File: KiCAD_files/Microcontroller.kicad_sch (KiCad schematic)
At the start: 71 parts, among them J403 RJ45_LED_Shielded, J404 RJ45_LED_Shielded, J405 Conn_01x02_Male, J406 Conn_01x02_Male, P401 Power2, U401 OwnTech_SPIN, U402 TCAN334GDR, U405 LTC2850xS8, U406 MCP6487T-E/SN, U407 MCP6486UT-E/LT

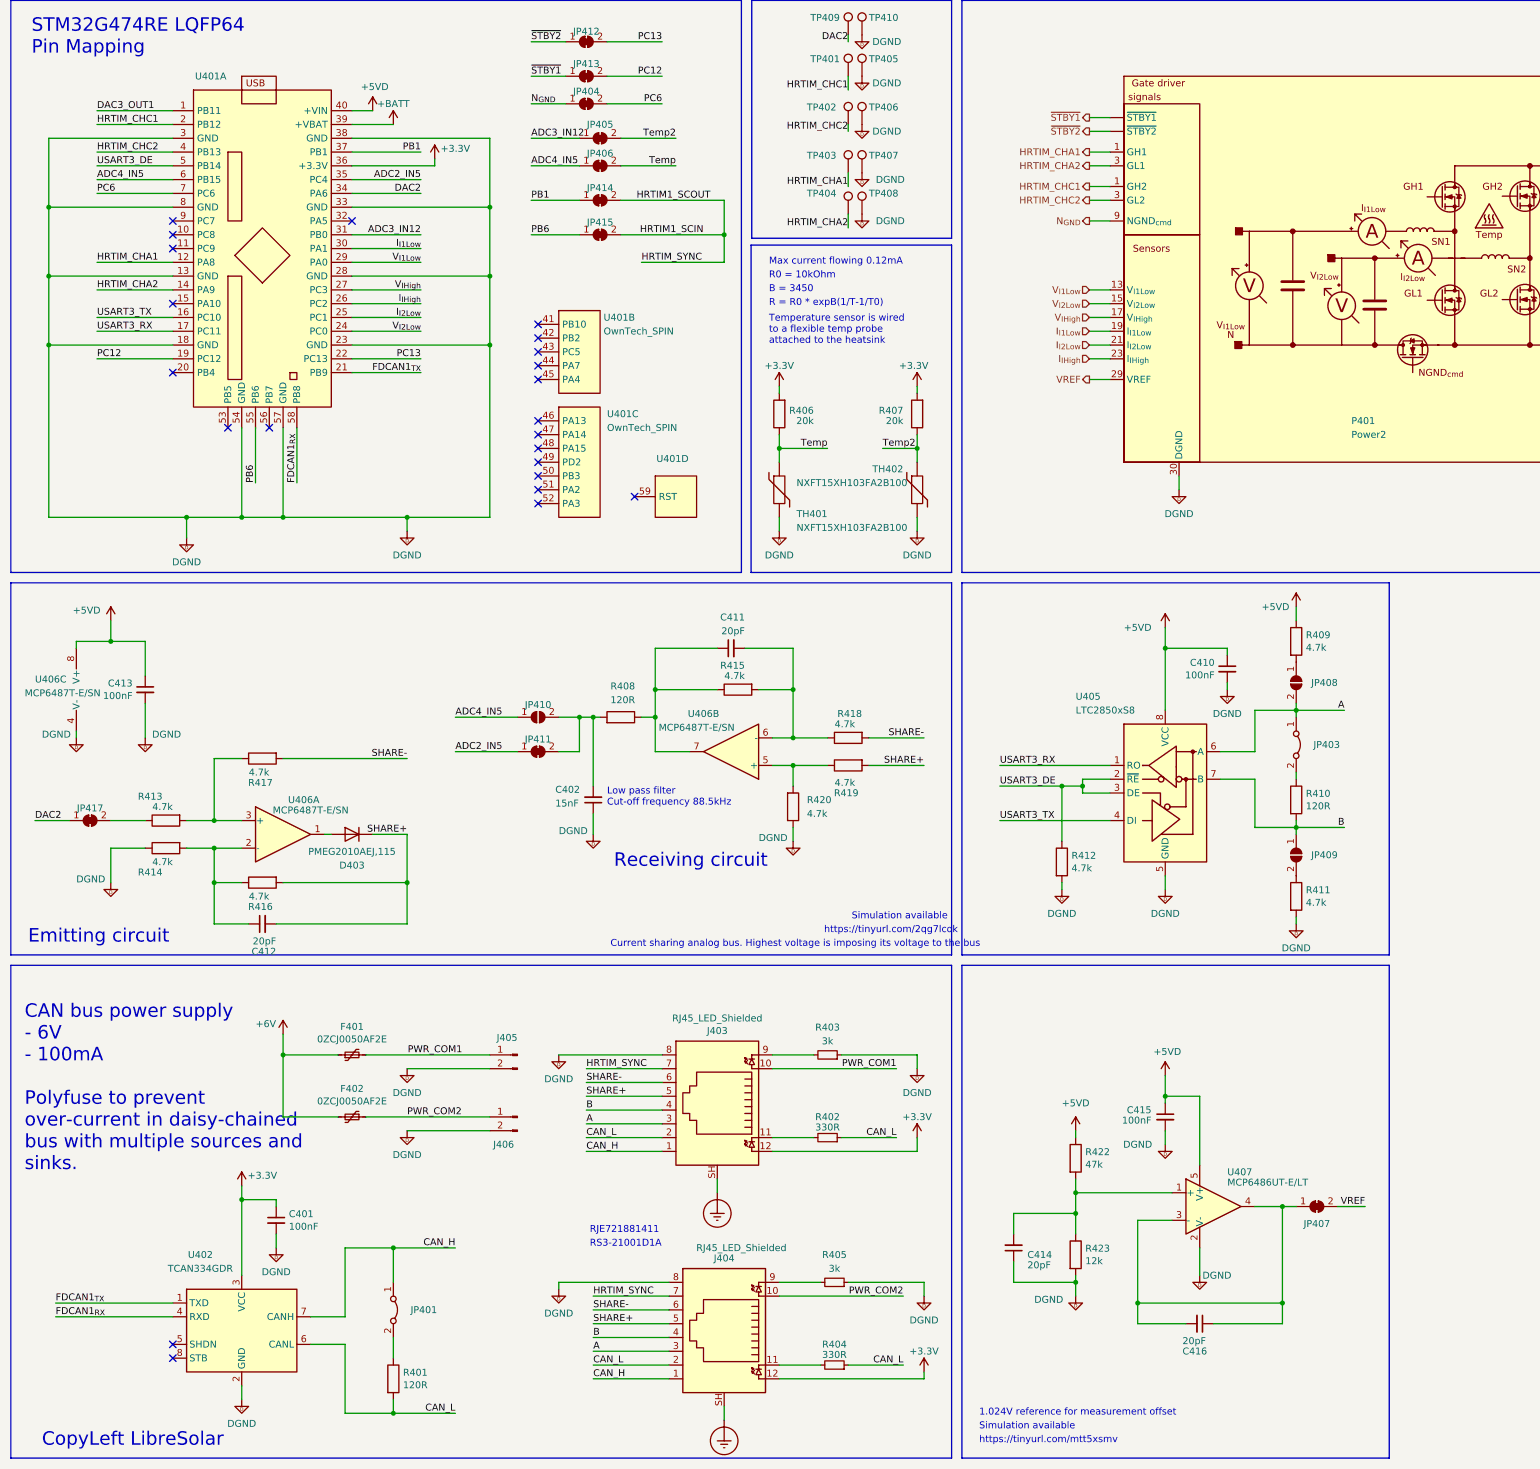
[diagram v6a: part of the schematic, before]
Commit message: Added metadata on components to define their functional group and sub-functions in order to permit contextualized hightlights in interactive BOM.
Signed-off-by: Jean Alinei <jean.alinei@laas.fr>
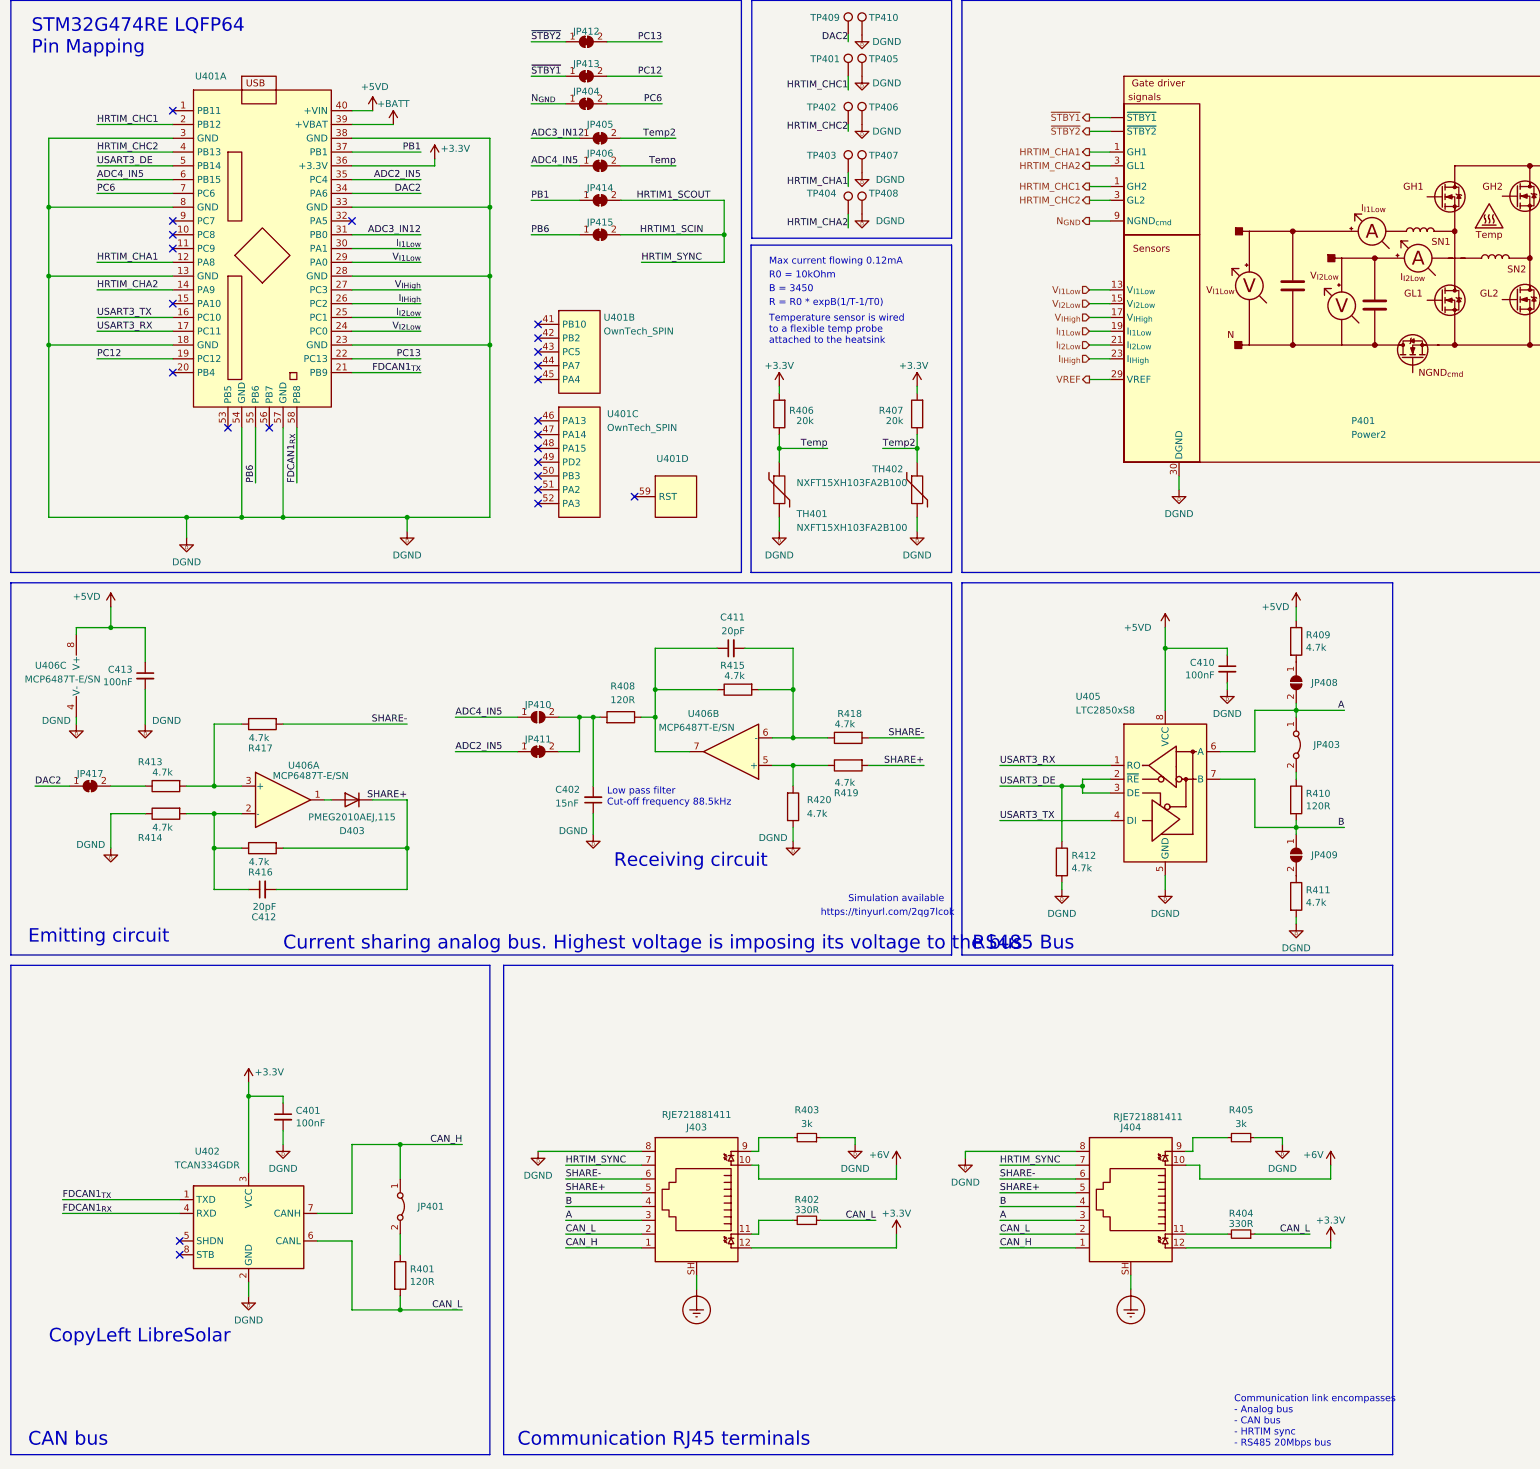
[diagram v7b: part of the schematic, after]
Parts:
- removed C414, C416: 20pF, Footprints:C_0805_2012Metric, symbol Device:C_Small
- removed C415: 100nF, Footprints:C_0805_2012Metric, symbol Device:C_Small
- removed F401, F402: 0ZCJ0050AF2E, Fuse:Fuse_1210_3225Metric, symbol Device:Polyfuse_Small
- removed J405, J406: Conn_01x02_Male, Connector_JST:JST_EH_B2B-EH-A_1x02_P2.50mm_Vertical, symbol Connector:Conn_01x02_Male
- removed JP407: SolderJumper, Jumper:SolderJumper-2_P1.3mm_Bridged_RoundedPad1.0x1.5mm, symbol Jumper:SolderJumper_2_Bridged
- removed R422: 47k, Footprints:R_0805_2012Metric, symbol Device:R
- removed R423: 12k, Footprints:R_0805_2012Metric, symbol Device:R
- removed U407: MCP6486UT-E/LT, Package_TO_SOT_SMD:SOT-353_SC-70-5_Handsoldering, symbol Amplifier_Operational:TLV6001DCK
- C401: DNP x -> (none); Functional Block (none) -> Communication; Manf# C0805C104K5RACTU -> (none); Metal content (none) -> BaTiO3; Subfunction (none) -> CAN bus; manf# (none) -> C0805C104K5RACTU
- C402, C411, C412: DNP x -> (none); Functional Block (none) -> Communication; Manf# CC0805JRNPO9BN200 -> (none); Metal content (none) -> BaTiO3; Subfunction (none) -> Analog bus; manf# (none) -> CC0805JRNPO9BN200
- C410: #manf C1206C104K5RAC7867 -> (none); DNP x -> (none); Functional Block (none) -> Communication; Manf# C1206C104K5RAC7867 -> (none); Metal content (none) -> BaTiO3; Subfunction (none) -> RS485 bus; manf# (none) -> C1206C104K5RAC7867
- C413: DNP x -> (none); Functional Block (none) -> Communication; Manf# C0805C104K5RACTU -> (none); Metal content (none) -> BaTiO3; Subfunction (none) -> Analog bus; manf# (none) -> C0805C104K5RACTU
- D403: DNP x -> (none); Functional Block (none) -> Communication; Manf# PMEG2010AEJ,115 -> (none); Subfunction (none) -> Analog bus; manf# (none) -> PMEG2010AEJ,115
- J403, J404: value RJ45_LED_Shielded -> RJE721881411; DNP x -> (none); Functional Block (none) -> Communication; Manf# RJE721881411 -> (none); Subfunction (none) -> RJ45 Connector; manf# (none) -> RJE721881411
- JP401: Functional Block (none) -> Communication; Subfunction (none) -> CAN bus
- JP403, JP408, JP409: Functional Block (none) -> Communication; Subfunction (none) -> RS485 bus
- JP404: Functional Block (none) -> Driver; Subfunction (none) -> NGND driver
- JP405, JP406: Functional Block (none) -> Measurement; Subfunction (none) -> Temp measure
- JP410, JP411, JP417: Functional Block (none) -> Communication; Subfunction (none) -> Analog bus
- JP412, JP413: Functional Block (none) -> Driver; Subfunction (none) -> STBY driver
- JP414, JP415: Functional Block (none) -> Communication; Subfunction (none) -> HRTIM Sync
- R401: DNP x -> (none); Functional Block (none) -> Communication; Manf# CR0805-FX-1200ELF -> (none); Metal content (none) -> NiCr; Subfunction (none) -> CAN bus; manf# (none) -> CR0805-FX-1200ELF
- R402, R404: DNP x -> (none); Functional Block (none) -> Communication; Manf# CR0805-FX-3300ELF -> (none); Metal content (none) -> NiCr; Subfunction (none) -> RJ45 Connector; manf# (none) -> CR0805-FX-3300ELF
- R403, R405: DNP x -> (none); Functional Block (none) -> Communication; Manf# CR0805-FX-3001ELF -> (none); Metal content (none) -> NiCr; Subfunction (none) -> RJ45 Connector; manf# (none) -> CR0805-FX-3001ELF
- R406, R407: DNP x -> (none); Functional Block (none) -> Measurment; Manf# CR0805-FX-2002ELF -> (none); Metal content (none) -> NiCr; Subfunction (none) -> Temp Measure; manf# (none) -> CR0805-FX-2002ELF
- R408, R413, R414, R415, R416, R417, R418, R419, R420: DNP x -> (none); Functional Block (none) -> Communication; Manf# CR0805-FX-4701ELF -> (none); Metal content (none) -> NiCr; Subfunction (none) -> Analog bus; manf# (none) -> CR0805-FX-4701ELF
- R409, R411, R412: DNP x -> (none); Functional Block (none) -> Communication; Manf# CR0805-FX-4701ELF -> (none); Metal content (none) -> NiCr; Subfunction (none) -> RS485 bus; manf# (none) -> CR0805-FX-4701ELF
- R410: DNP x -> (none); Functional Block (none) -> Communication; Manf# CR0805-FX-1200ELF -> (none); Metal content (none) -> NiCr; Subfunction (none) -> RS485 bus; manf# (none) -> CR0805-FX-1200ELF
- TH401, TH402: DNP x -> (none); Manf# NXFT15XH103FA2B100 -> (none); Subfunction (none) -> Temp Measure; manf# (none) -> NXFT15XH103FA2B100
- U401: Functional Block (none) -> Microcontroller
- U402: DNP x -> (none); Functional Block (none) -> Communication; Manf# TCAN334GDR -> (none); Subfunction (none) -> CAN bus; manf# (none) -> TCAN334GDR
- U405: DNP x -> (none); Functional Block (none) -> Communication; Manf# LTC2850CS8#PBF -> (none); Subfunction (none) -> RS485 bus; manf# (none) -> LTC2850CS8#PBF
- U406: DNP x -> (none); Functional Block (none) -> Communication; Manf# MCP6487T-E/SN -> (none); Subfunction (none) -> Analog bus; manf# (none) -> MCP6487T-E/SN
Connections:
- net PWR_COM1 is gone; now on net +6V: J403.10
- net PWR_COM2 is gone; now on net +6V: J404.10
- net DAC3_OUT1: no longer names the net of U401.1 (PB11)
- no-connect marks 23 -> 24
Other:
- note added: "CAN bus"
- note added: "Communication RJ45 terminals"
- note added: "Communication link encompasses - Analog bus - CAN bus - HRTIM sync - RS485 20Mbps bus"
- note added: "RS485 Bus"
- note removed: "1.024V reference for measurement offset"
- note removed: "CAN bus power supply - 6V - 100mA Polyfuse to prevent over-current in daisy-chained bus with multiple sources and sinks."
- note removed: "RJE721881411"
- note removed: "RS3-21001D1A"
- note removed: "https://tinyurl.com/mtt5xsmv"
- moved on the sheet: C401, C412, C413, D403, J403, J404, JP401, JP417, R401, R402, R403, R404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

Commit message: modified some functions and subfunctions
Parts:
- JP405, JP406: Subfunction Temp measure -> Temp Measure
- R406, R407: Functional Block Measurment -> Measurement
- TH401, TH402: Functional Block (none) -> Measurement
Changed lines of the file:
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@@
       (effects (font (size 1.27 1.27)) hide)
     )
-    (property "Functional Block" "" (at 168.91 104.14 0)
+    (property "Functional Block" "Measurement" (at 168.91 104.14 0)
       (effects (font (size 1.27 1.27)) hide)
     )
@@
       (effects (font (size 1.27 1.27)) hide)
     )
-    (property "Functional Block" "Measurment" (at 168.91 90.17 0)
+    (property "Functional Block" "Measurement" (at 168.91 90.17 0)
       (effects (font (size 1.27 1.27)) hide)
     )
@@
       (effects (font (size 1.27 1.27)) hide)
     )
-    (property "Subfunction" "Temp measure" (at 135.89 39.37 0)
+    (property "Subfunction" "Temp Measure" (at 135.89 39.37 0)
       (effects (font (size 1.27 1.27)) hide)
     )
@@
       (effects (font (size 1.27 1.27)) hide)
     )
-    (property "Functional Block" "" (at 194.31 104.14 0)
+    (property "Functional Block" "Measurement" (at 194.31 104.14 0)
       (effects (font (size 1.27 1.27)) hide)
     )
@@
       (effects (font (size 1.27 1.27)) hide)
     )
-    (property "Subfunction" "Temp measure" (at 135.89 44.45 0)
+    (property "Subfunction" "Temp Measure" (at 135.89 44.45 0)
       (effects (font (size 1.27 1.27)) hide)
     )
@@
       (effects (font (size 1.27 1.27)) hide)
     )
-    (property "Functional Block" "Measurment" (at 194.31 90.17 0)
+    (property "Functional Block" "Measurement" (at 194.31 90.17 0)
       (effects (font (size 1.27 1.27)) hide)
     )
